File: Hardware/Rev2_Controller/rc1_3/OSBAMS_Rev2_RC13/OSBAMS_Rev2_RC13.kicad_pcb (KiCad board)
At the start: 4 copper layers, 100 x 90 mm, 154 parts, among them J1 12V_IN, J2 ESTOP, J3 ARM, J4 K1_COIL, J5 SHUNT_KELVIN, J6 PACK_SENSE, J7 TEMP_PROBE, J8 USB-C HOST, J9 SWD, Q1 IRLML0060, SW1 RESET, U1 STM32L476RGT6, U10 USBLC6-2SC6, U2 INA228, U3 LMR14006Y, U4 VO610A-1, U5 VO610A-1, U6 CP2102N, U7 ISO7721, U9 USBLC6-2SC6

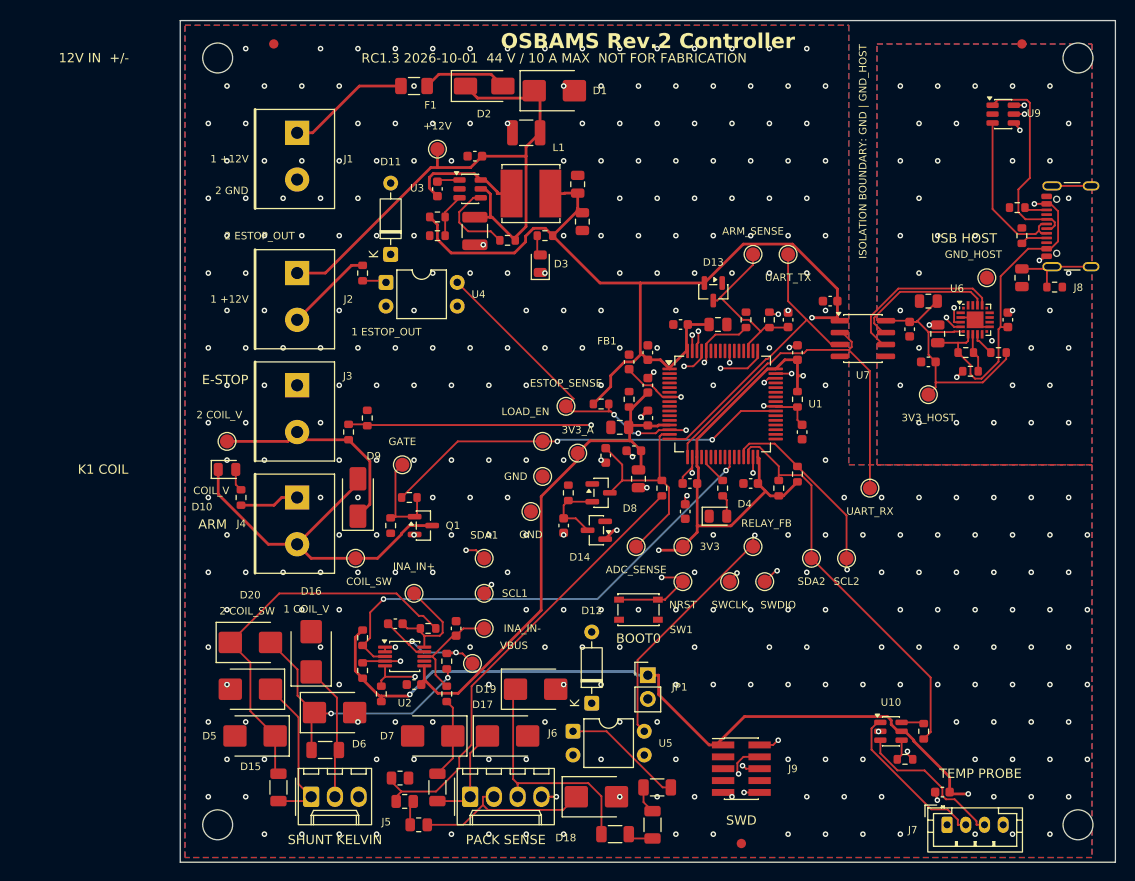
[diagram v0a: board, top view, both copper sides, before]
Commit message: Controller RC1.3: exact Samtec FTSH-105-01-L-DV-K footprint (drawing rev H), verified 1.5SMBJ12CA data, rerouted; checks clean
Co-Authored-By: Claude Sonnet 5.5 <noreply@anthropic.com>
Claude-Session: https://claude.ai/code/session_01ENatZXrEDA18PaxUrZWrpi
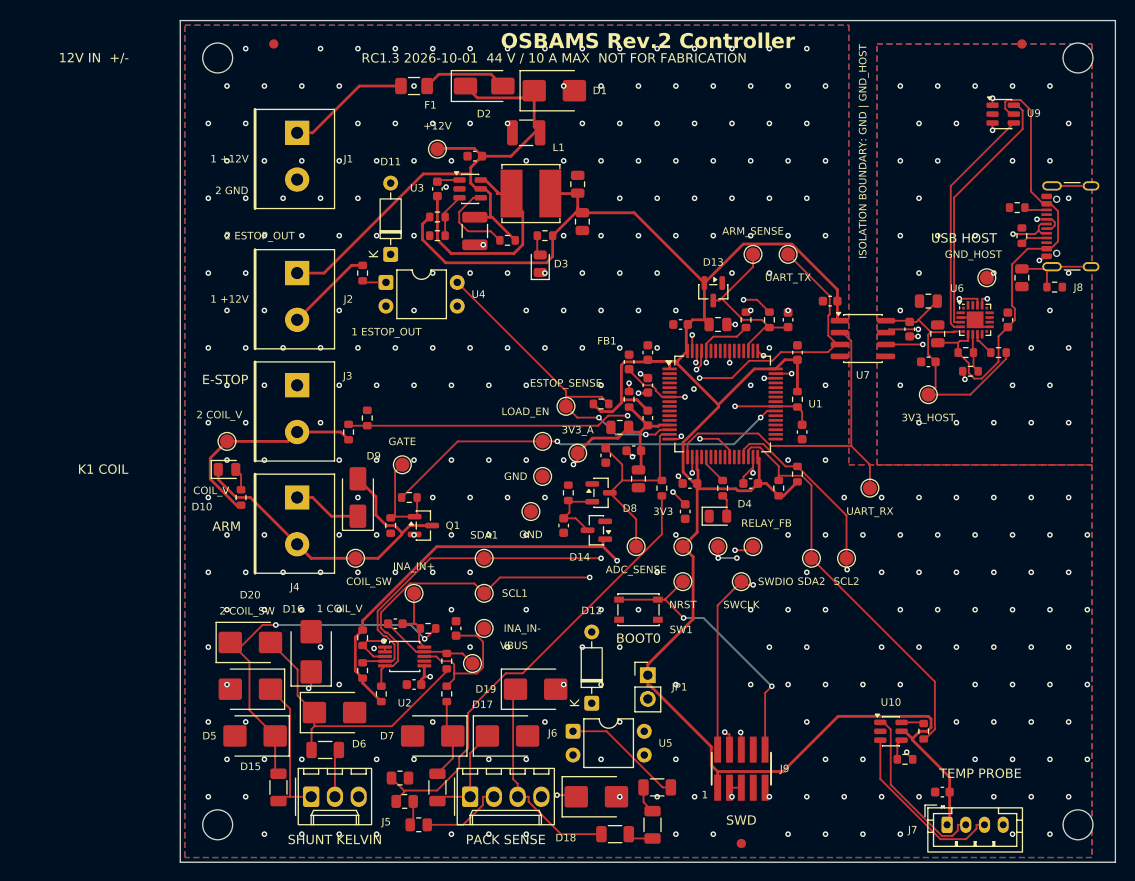
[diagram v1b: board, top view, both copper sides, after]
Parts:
- J9: footprint Connector_PinHeader_1.27mm:PinHeader_2x05_P1.27mm_Vertical_SMD -> OSBAMS_Rev2:FTSH-105-01-L-DV-K
- moved TP24 3.95 mm to (157.5, 116.2)
- moved TP23 2.50 mm to (160.0, 120.0)
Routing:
- net BUCK_SW: track 12.3 -> 25.1 mm
- net SCL1: track 54.9 -> 63.9 mm, vias 3 -> 2
- net INA_ALERT: track 52.7 -> 58.5 mm
- net 3V3_A: track 57.9 -> 63.3 mm, vias 0 -> 3
- net INA_VBUS: track 11.5 -> 16.5 mm
- net SHUNT_INN_CON: track 14.8 -> 19.8 mm, vias 0 -> 1
- net UART_TX_MCU: track 32.4 -> 37.2 mm, vias 0 -> 2
- net +12V: track 66.3 -> 61.9 mm
- net INA_INN: track 15.0 -> 10.8 mm, vias 2 -> 0
- net INA_INP: track 11.9 -> 7.65 mm
- net UART_RX_HOST: track 18.2 -> 14.1 mm, vias 0 -> 2
- net SDA1: track 58.3 -> 62.2 mm, vias 3 -> 2
- net SWO: track 46.9 -> 43.3 mm
- net UART_TX_HOST: track 15.5 -> 12.0 mm, vias 0 -> 2
- net SWCLK: track 54.5 -> 51.3 mm, vias 3 -> 4
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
